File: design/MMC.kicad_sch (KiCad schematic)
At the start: 58 parts

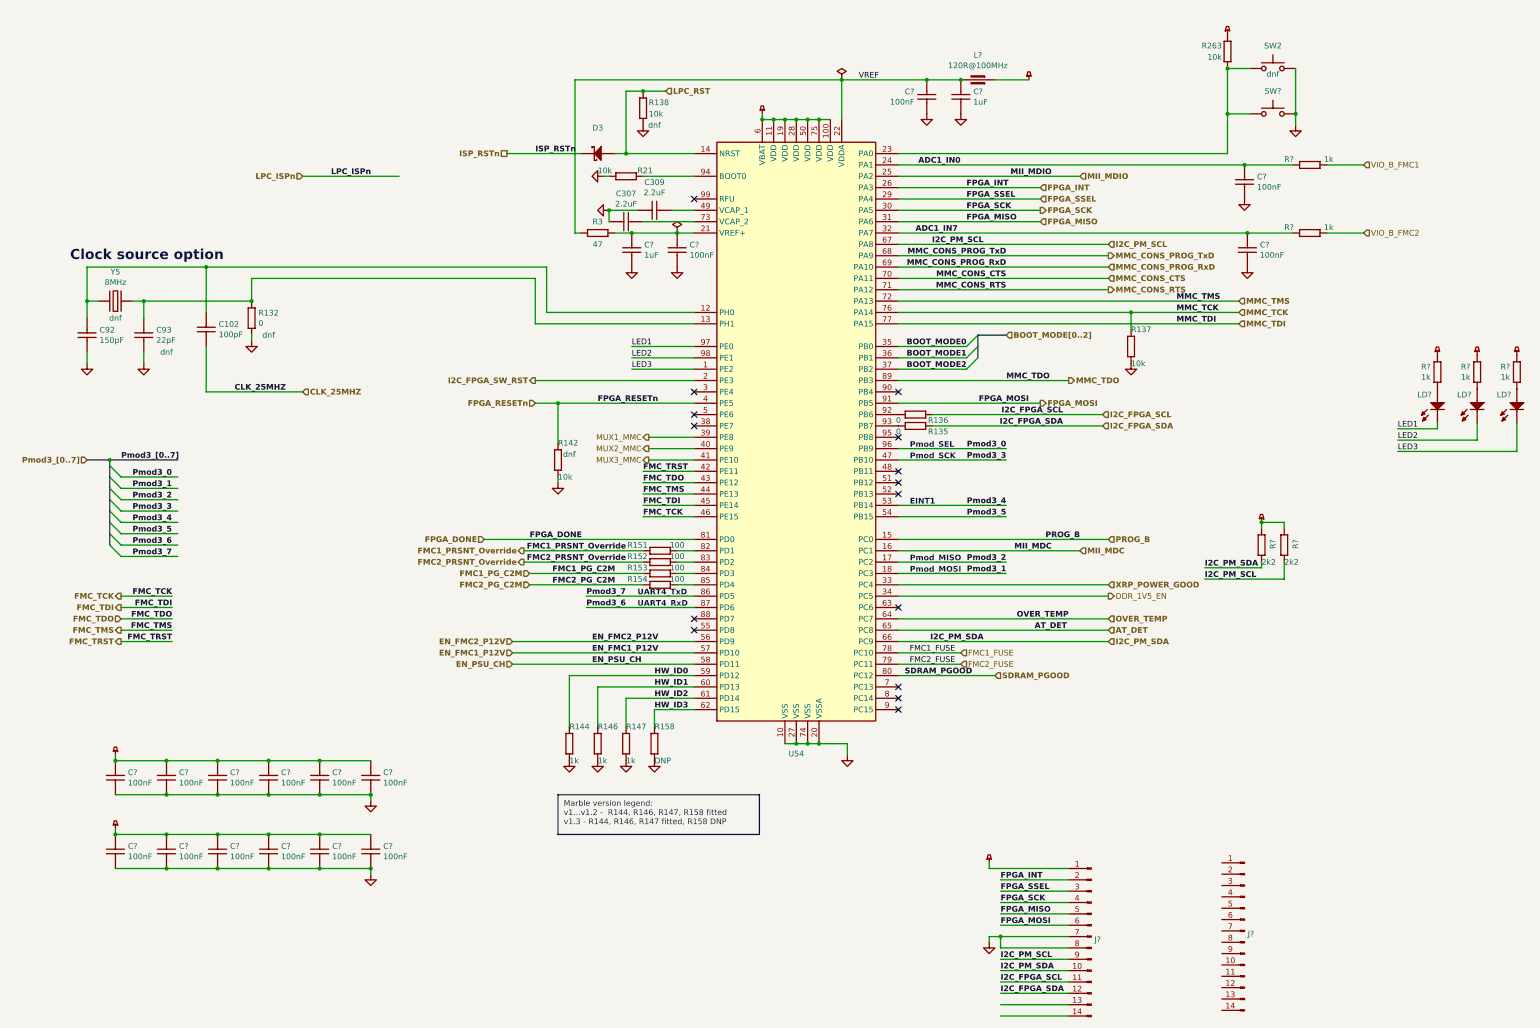
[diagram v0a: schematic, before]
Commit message: new power converter added
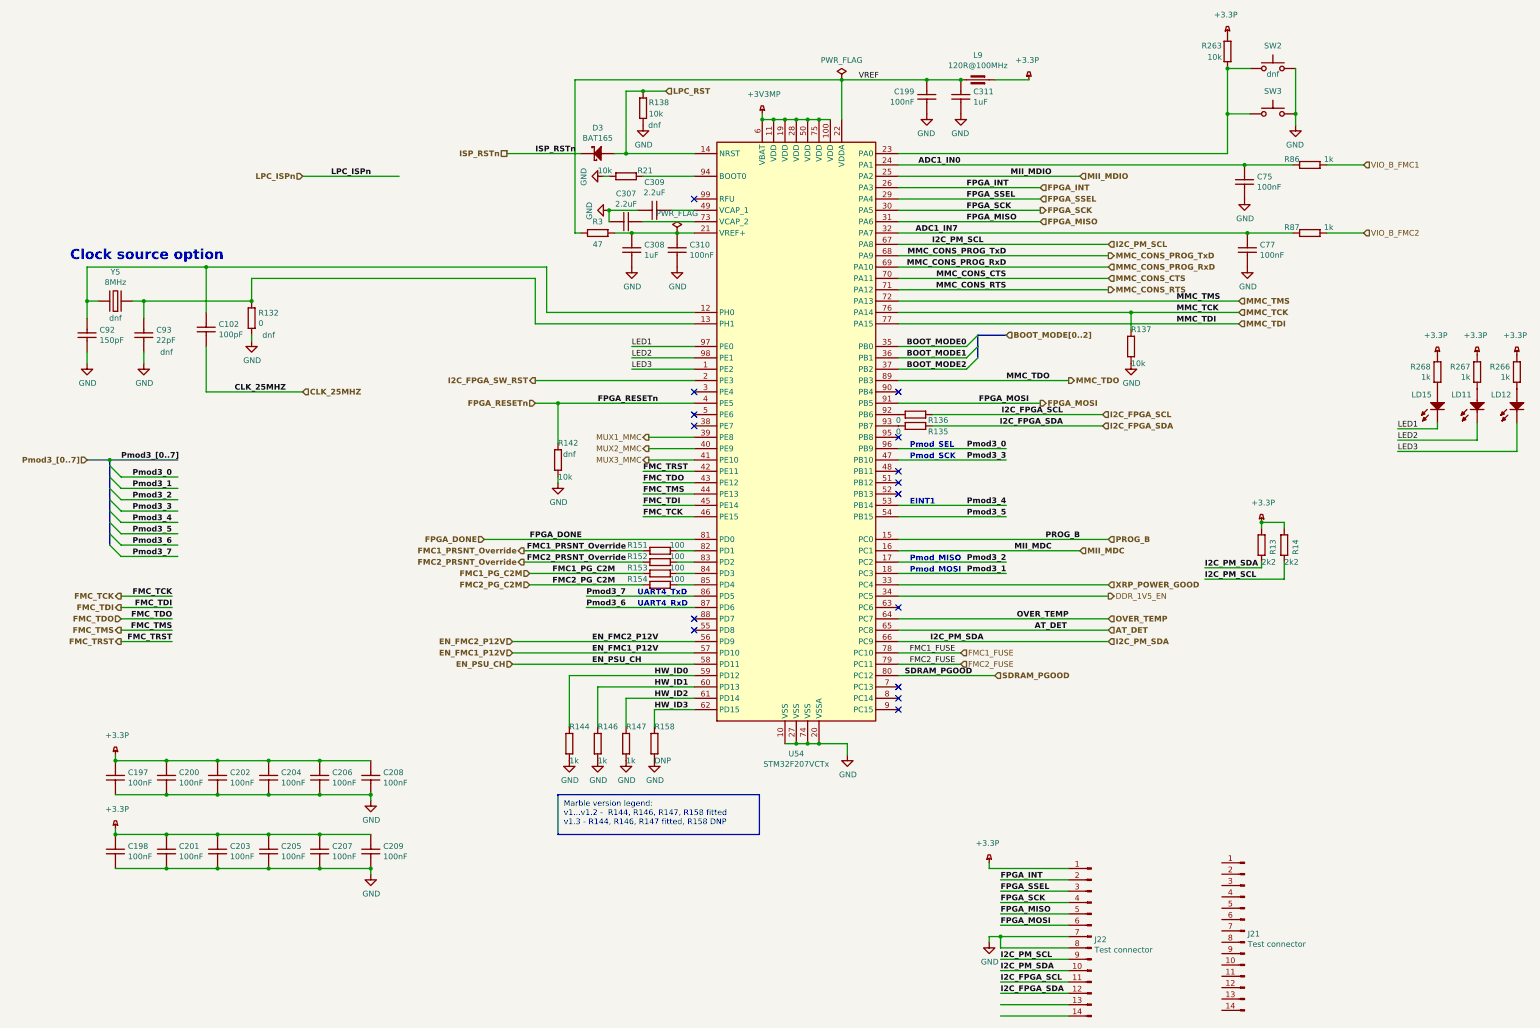
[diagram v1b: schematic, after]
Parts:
- C102: value (none) -> CC0402_100PF_50V_5%_C0G; footprint (none) -> Capacitors SMD:CAPC1005X55N
- C197, C198, C199, C200, C201, C202, C203, C204, C205, C206, C207, C208, C209, C310, C75, C77: renamed from C?; value (none) -> CC0201_100NF_6.3V_10%_X5R; footprint (none) -> CAPC0603X33N
- C307, C309: value (none) -> CC0402_2.2UF_6.3V_10%_X5R; footprint (none) -> Capacitors SMD:CAPC1005X55N
- C308, C311: renamed from C?; value (none) -> CC0402_1UF_16V_10%_X5R; footprint (none) -> Capacitors SMD:CAPC1005X55N
- C92: value (none) -> CC0402_150PF_50V_5%_C0G; footprint (none) -> CAPC1005X55N
- C93: value (none) -> CC0402_22PF_50V_5%_C0G; footprint (none) -> CAPC1005X55N
- D3: value (none) -> BAT165; footprint (none) -> ICs And Semiconductors SMD:SOD2512X110N
- J21: renamed from J?; value (none) -> Test connector; footprint (none) -> Connector:Tag-Connect_TC2070-IDC-FP_2x07_P1.27mm_Vertical
- J22: renamed from J?; value (none) -> Test connector; footprint (none) -> Connector_PinSocket_2.54mm:PinSocket_1x14_P2.54mm_Vertical_SMD_Pin1Left
- L9: renamed from L?; value (none) -> IND0603_MURATA_BLM18SG121TN1D; footprint (none) -> INDC1608X65N
- LD11, LD12, LD15: renamed from LD?; value (none) -> LED_KINGBRIGHT_KPH-1608CGCK; footprint (none) -> ICs And Semiconductors SMD:LED_KINGBRIGHT_KPH-1608CGCK
- R13, R14: renamed from R?; value (none) -> R0402_2K2_1%_0.0625W_100PPM; footprint (none) -> RESC1005X40N
- R132, R135, R136: value (none) -> R0402_0R_JUMPER; footprint (none) -> RESC1005X40N
- R137, R138, R142, R21, R263: value (none) -> R0402_10K_1%_0.0625W_100PPM; footprint (none) -> RESC1005X40N
- R144, R146, R147, R158: value (none) -> R0402_1K_1%_0.0625W_100PPM; footprint (none) -> RESC1005X40N
- R151, R152, R153, R154: value (none) -> R0402_100R_1%_0.1W_100PPM; footprint (none) -> RESC1005X40N
- R266, R267, R268, R86, R87: renamed from R?; value (none) -> R0402_1K_1%_0.0625W_100PPM; footprint (none) -> RESC1005X40N
- R3: value (none) -> R0603_47R_1%_0.1W_100PPM; footprint (none) -> Resistors SMD:RESC1608X55N
- SW2: value (none) -> SKHHLQA010; footprint (none) -> Switches:PB_ALPS_SKHHLQA010
- SW3: renamed from SW?; value (none) -> KSS241GLFS; footprint (none) -> Marble:KSS241GLFS
- U54: value (none) -> STM32F207VCTx; footprint (none) -> Package_QFP:LQFP-100_14x14mm_P0.5mm
- Y5: value (none) -> XTAL_8MHZ_TXC_7A-8.000MAAE-T; footprint (none) -> XTAL_TXC_7A

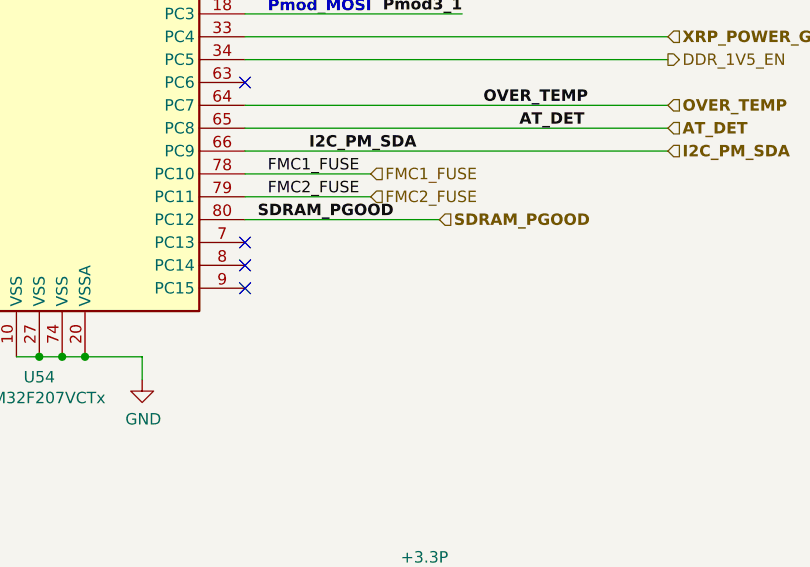
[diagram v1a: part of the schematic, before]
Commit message: LTM4673 control signals connected to MMC
LTM4673 control signals connected to MMC
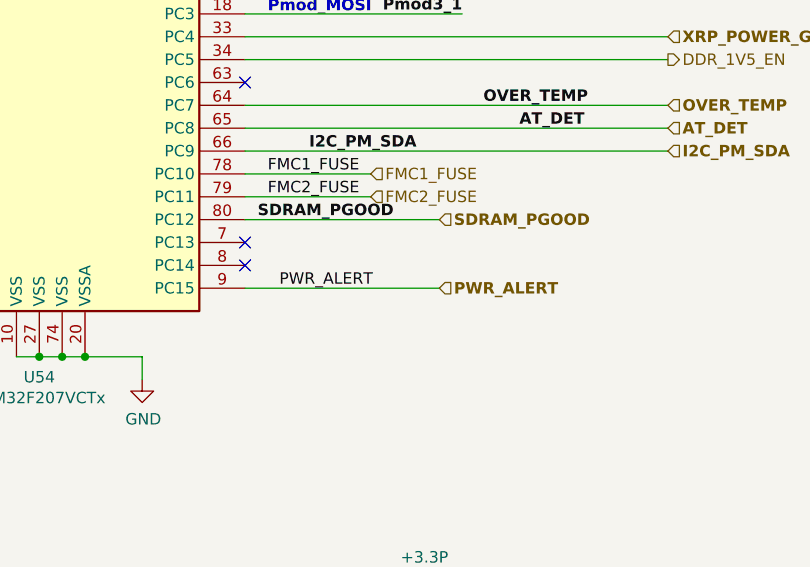
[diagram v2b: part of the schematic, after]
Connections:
- net PWR_ALERT: now reaches U54.9 (PC15)
- no-connect marks 15 -> 14
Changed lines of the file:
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@@
   (no_connect (at 219.71 124.46))
   (no_connect (at 173.99 58.42))
-  (no_connect (at 219.71 172.72))
   (no_connect (at 173.99 101.6))
   (bus_entry (at 43.18 128.27) (size 2.54 2.54)
@@
   )
   (wire (pts (xy 243.84 139.7) (xy 219.71 139.7))
+    (stroke (width 0) (type default) (color 0 0 0 0))
+  )
+  (wire (pts (xy 219.71 172.72) (xy 241.3 172.72))
     (stroke (width 0) (type default) (color 0 0 0 0))
   )
@@
     (effects (font (size 1.27 1.27) (thickness 0.254) bold) (justify right bottom))
   )
+  (label "PWR_ALERT" (at 223.52 172.72 0)
+    (effects (font (size 1.27 1.27)) (justify left bottom))
+  )
   (label "LPC_ISPn" (at 92.71 53.34 0)
     (effects (font (size 1.27 1.27) (thickness 0.254) bold) (justify left bottom))
@@
     (effects (font (size 1.27 1.27) (thickness 0.254) bold) (justify left))
   )
+  (hierarchical_label "PWR_ALERT" (shape input) (at 241.3 172.72 0)
+    (effects (font (size 1.27 1.27) (thickness 0.254) bold) (justify left))
+  )

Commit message: connected signals to the J9 connector
connected signals to the J9 connector
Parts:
- C102, C197, C198, C199, C200, C201, C202, C203, C204, C205, C206, C207, C208, C209, C308, C310, C311, C75, C77, C92, C93, L9, R13, R132, R135, R136, R137, R138, R14, R142, R144, R146, R147, R151, R152, R153, R154, R158, R21, R263, R266, R267, R268, R3, R86, R87: Author CERN DEM JLC -> (none)
- C307, C309: Author CERN DEM JMW -> (none)
- D3, Y5: Author CERN DEM JLC -> (none); Bonding No -> (none)
- LD11, LD12, LD15: Author CERN DEM JLC -> (none); Bonding No -> (none); Color Green -> (none)

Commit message: Attempt to add and improve BOM. Added new part numbers for some of the passives
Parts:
- C307, C308, C309, C311, C92, C93, R132, R135, R136: MANUFACTURER (none) -> GENERIC
- R151, R152, R153, R154: MANUFACTURER (none) -> GENERIC; Manufacturer Part Number R0402_100R_1%_0.1W_100PPM_50V -> R0402_100R_1%_0.1W_100PPM
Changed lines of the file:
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@@
     )
     (property "config" "dnf" (id 40) (at 55.88 92.71 90))
+    (property "MANUFACTURER" "GENERIC" (id 41) (at 50.8 85.09 0)
+      (effects (font (size 1.27 1.27)) hide)
+    )
     (pin "1")
     (pin "2")
@@
       (effects (font (size 1.524 1.524)) (justify left) hide)
     )
+    (property "MANUFACTURER" "GENERIC" (id 41) (at 227.33 109.22 0)
+      (effects (font (size 1.27 1.27)) hide)
+    )
     (pin "1")
     (pin "2")
@@
       (effects (font (size 1.524 1.524)) (justify left) hide)
     )
+    (property "MANUFACTURER" "GENERIC" (id 41) (at 227.33 106.68 0)
+      (effects (font (size 1.27 1.27)) hide)
+    )
     (pin "1")
     (pin "2")
@@
     )
     (property "config" "dnf" (id 41) (at 78.74 88.9 90))
+    (property "MANUFACTURER" "GENERIC" (id 42) (at 74.93 81.28 0)
+      (effects (font (size 1.27 1.27)) hide)
+    )
     (pin "1")
     (pin "2")
@@
       (effects (font (size 1.524 1.524)) (justify left) hide)
     )
-    (property "Manufacturer Part Number" "R0402_100R_1%_0.1W_100PPM_50V" (id 23) (at 162.56 192.786 0)
+    (property "Manufacturer Part Number" "R0402_100R_1%_0.1W_100PPM" (id 23) (at 162.56 192.786 0)
       (effects (font (size 1.524 1.524)) (justify left) hide)
     )
@@
       (effects (font (size 1.524 1.524)) (justify left) hide)
     )
+    (property "MANUFACTURER" "GENERIC" (id 41) (at 162.56 137.16 0)
+      (effects (font (size 1.27 1.27)) hide)
+    )
     (pin "1")
     (pin "2")
@@
       (effects (font (size 1.524 1.524)) (justify left) hide)
     )
-    (property "Manufacturer Part Number" "R0402_100R_1%_0.1W_100PPM_50V" (id 23) (at 162.56 195.326 0)
+    (property "Manufacturer Part Number" "R0402_100R_1%_0.1W_100PPM" (id 23) (at 162.56 195.326 0)
       (effects (font (size 1.524 1.524)) (justify left) hide)
     )
@@
       (effects (font (size 1.524 1.524)) (justify left) hide)
     )
+    (property "MANUFACTURER" "GENERIC" (id 41) (at 162.56 139.7 0)
+      (effects (font (size 1.27 1.27)) hide)
+    )
     (pin "1")
     (pin "2")
@@
       (effects (font (size 1.524 1.524)) (justify left) hide)
     )
-    (property "Manufacturer Part Number" "R0402_100R_1%_0.1W_100PPM_50V" (id 23) (at 162.56 197.866 0)
+    (property "Manufacturer Part Number" "R0402_100R_1%_0.1W_100PPM" (id 23) (at 162.56 197.866 0)
       (effects (font (size 1.524 1.524)) (justify left) hide)
     )
@@
       (effects (font (size 1.524 1.524)) (justify left) hide)
     )
+    (property "MANUFACTURER" "GENERIC" (id 41) (at 162.56 142.24 0)
+      (effects (font (size 1.27 1.27)) hide)
+    )
     (pin "1")
     (pin "2")
@@
       (effects (font (size 1.524 1.524)) (justify left) hide)
     )
-    (property "Manufacturer Part Number" "R0402_100R_1%_0.1W_100PPM_50V" (id 23) (at 162.56 200.406 0)
+    (property "Manufacturer Part Number" "R0402_100R_1%_0.1W_100PPM" (id 23) (at 162.56 200.406 0)
       (effects (font (size 1.524 1.524)) (justify left) hide)
     )
@@
       (effects (font (size 1.524 1.524)) (justify left) hide)
     )
+    (property "MANUFACTURER" "GENERIC" (id 41) (at 162.56 144.78 0)
+      (effects (font (size 1.27 1.27)) hide)
+    )
     (pin "1")
     (pin "2")
@@
       (effects (font (size 1.524 1.524)) (justify left) hide)
     )
+    (property "MANUFACTURER" "GENERIC" (id 40) (at 38.1 85.09 0)
+      (effects (font (size 1.27 1.27)) hide)
+    )
     (pin "1")
     (pin "2")
@@
       (effects (font (size 1.27 1.27)) (justify left) hide)
     )
+    (property "MANUFACTURER" "GENERIC" (id 39) (at 161.29 60.96 0)
+      (effects (font (size 1.27 1.27)) hide)
+    )
     (pin "1")
     (pin "2")
@@
       (effects (font (size 1.27 1.27)) (justify left) hide)
     )
+    (property "MANUFACTURER" "GENERIC" (id 39) (at 154.94 63.5 0)
+      (effects (font (size 1.27 1.27)) hide)
+    )
     (pin "1")
     (pin "2")
@@
       (effects (font (size 1.27 1.27)) (justify left) hide)
     )
+    (property "MANUFACTURER" "GENERIC" (id 39) (at 233.68 31.75 0)
+      (effects (font (size 1.27 1.27)) hide)
+    )
     (pin "1")
     (pin "2")
@@
       (effects (font (size 1.27 1.27)) (justify left) hide)
     )
+    (property "MANUFACTURER" "GENERIC" (id 39) (at 160.02 66.04 0)
+      (effects (font (size 1.27 1.27)) hide)
+    )
     (pin "1")

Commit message: no ERC issues
no ERC issues
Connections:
- net PWR_RESET: now reaches U54.8 (PC14)
- no-connect marks 14 -> 29
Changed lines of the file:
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@@
   (junction (at 55.88 208.28) (diameter 0) (color 0 0 0 0)
   )
-  (no_connect (at 219.71 170.18))
   (no_connect (at 173.99 106.68))
   (no_connect (at 219.71 167.64))
   (no_connect (at 219.71 121.92))
   (no_connect (at 219.71 111.76))
+  (no_connect (at 257.81 241.3))
+  (no_connect (at 257.81 238.76))
+  (no_connect (at 292.1 219.71))
+  (no_connect (at 292.1 222.25))
+  (no_connect (at 292.1 224.79))
+  (no_connect (at 292.1 232.41))
+  (no_connect (at 292.1 237.49))
+  (no_connect (at 292.1 234.95))
+  (no_connect (at 292.1 227.33))
+  (no_connect (at 292.1 229.87))
+  (no_connect (at 292.1 240.03))
+  (no_connect (at 292.1 217.17))
+  (no_connect (at 292.1 214.63))
+  (no_connect (at 292.1 212.09))
+  (no_connect (at 292.1 209.55))
+  (no_connect (at 292.1 207.01))
   (no_connect (at 219.71 101.6))
   (no_connect (at 173.99 152.4))
@@
     (stroke (width 0) (type default) (color 0 0 0 0))
   )
-  (wire (pts (xy 242.57 241.3) (xy 257.81 241.3))
-    (stroke (width 0) (type default) (color 0 0 0 0))
-  )
   (wire (pts (xy 44.45 200.66) (xy 55.88 200.66))
     (stroke (width 0) (type default) (color 0 0 0 0))
@@
     (stroke (width 0) (type default) (color 0 0 0 0))
   )
-  (wire (pts (xy 242.57 238.76) (xy 257.81 238.76))
-    (stroke (width 0) (type default) (color 0 0 0 0))
-  )
   (wire (pts (xy 148.59 66.04) (xy 147.32 66.04))
     (stroke (width 0) (type default) (color 0 0 0 0))
@@
     (stroke (width 0) (type default) (color 0 0 0 0))
   )
-  (wire (pts (xy 86.36 53.34) (xy 107.95 53.34))
-    (stroke (width 0) (type default) (color 0 0 0 0))
-  )
   (wire (pts (xy 219.71 83.82) (xy 271.78 83.82))
     (stroke (width 0) (type default) (color 0 0 0 0))
@@
   )
   (wire (pts (xy 57.15 154.94) (xy 45.72 154.94))
+    (stroke (width 0) (type default) (color 0 0 0 0))
+  )
+  (wire (pts (xy 219.71 170.18) (xy 241.3 170.18))
     (stroke (width 0) (type default) (color 0 0 0 0))
   )
@@
     (effects (font (size 1.27 1.27)) (justify left bottom))
   )
-  (label "LPC_ISPn" (at 92.71 53.34 0)
-    (effects (font (size 1.27 1.27) (thickness 0.254) bold) (justify left bottom))
-  )
   (label "MMC_TCK" (at 281.94 83.82 0)
     (effects (font (size 1.27 1.27) (thickness 0.254) bold) (justify left bottom))
@@
     (effects (font (size 1.27 1.27) (thickness 0.254) bold) (justify right bottom))
   )
+  (label "PWR_RESET" (at 223.52 170.18 0)
+    (effects (font (size 1.27 1.27)) (justify left bottom))
+  )
   (label "FMC_TMS" (at 57.15 154.94 180)
     (effects (font (size 1.27 1.27) (thickness 0.254) bold) (justify right bottom))
@@
     (effects (font (size 1.27 1.27) (thickness 0.254) bold) (justify left))
   )
+  (hierarchical_label "PWR_RESET" (shape output) (at 241.3 170.18 0)
+    (effects (font (size 1.27 1.27) (thickness 0.254) bold) (justify left))
+  )
   (hierarchical_label "ISP_RSTn" (shape passive) (at 132.08 48.26 180)
     (effects (font (size 1.27 1.27) (thickness 0.254) bold) (justify right))
@@
     (effects (font (size 1.27 1.27) (thickness 0.254) bold) (justify right))
   )
-  (hierarchical_label "LPC_ISPn" (shape input) (at 86.36 53.34 180)
-    (effects (font (size 1.27 1.27) (thickness 0.254) bold) (justify right))
-  )
